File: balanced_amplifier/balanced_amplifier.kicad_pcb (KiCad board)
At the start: 2 copper layers, 100 x 100 mm, 124 parts, among them J1 Molex_SL_01x02_Male, J2 Molex_SL_01x02_Male, J3 Molex_SL_01x03_Male, J4 Molex_SL_01x02_Male, J5 Molex_SL_01x02_Male, J6 Molex_SL_01x02_Male, J7 Molex_SL_01x02_Male, U1 LM4562, U2 LM4562, U3 NE5532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

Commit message: update TODO and date in titleblock
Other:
- board text added: "TODO Update date silk Add license info to silk check pot directions update pot footprints (square pin 1, etc.)"
- board text removed: "TODO Update date silk Add license info to silk Update title block check pot directions update pot footprints (square pin 1, etc.)"
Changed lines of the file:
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@@
   (title_block
     (title "Balanced Amplifier")
-    (date 2019-06-18)
+    (date 2019-06-19)
     (rev 1)
     (company "G. Keeth")
@@
     (arrow2b (pts (xy 65.200001 33.8) (xy 65.786422 34.926504)))
   )
-  (gr_text "TODO\nUpdate date silk\nAdd license info to silk\nUpdate title block\ncheck pot directions\nupdate pot footprints (square pin 1, etc.)" (at 213.2 34.3) (layer Cmts.User)
+  (gr_text "TODO\nUpdate date silk\nAdd license info to silk\ncheck pot directions\nupdate pot footprints (square pin 1, etc.)" (at 213.2 34.3) (layer Cmts.User)
     (effects (font (size 1 1) (thickness 0.15)) (justify left))
   )
@@
   (segment (start 92.66 51.82) (end 93.765 52.925) (width 0.25) (layer F.Cu) (net 37))
   (segment (start 92.66 34.3) (end 92.66 51.82) (width 0.25) (layer F.Cu) (net 37))
-  (segment (start 144.385 48.425) (end 146.05 50.09) (width 0.25) (layer F.Cu) (net 58))
-  (segment (start 146.05 50.965) (end 142.875 54.14) (width 0.25) (layer F.Cu) (net 58))
-  (segment (start 146.05 50.09) (end 146.05 50.965) (width 0.25) (layer F.Cu) (net 58))
-  (segment (start 148.59 48.03) (end 148.985 48.425) (width 0.25) (layer F.Cu) (net 59))
-  (segment (start 147.32 50.09) (end 147.32 54.14) (width 0.25) (layer F.Cu) (net 59))
-  (segment (start 148.985 48.425) (end 147.32 50.09) (width 0.25) (layer F.Cu) (net 59))
-  (segment (start 167.005 50.725) (end 169.305 48.425) (width 0.25) (layer F.Cu) (net 61))
-  (segment (start 167.005 52.87) (end 167.005 50.725) (width 0.25) (layer F.Cu) (net 61))
-  (segment (start 160.96 48.195) (end 160.895 48.26) (width 0.25) (layer F.Cu) (net 60) (status 40000))
-  (segment (start 160.895 48.26) (end 161.76 48.26) (width 0.25) (layer F.Cu) (net 60))
-  (segment (start 162.56 49.06) (end 162.56 53.505) (width 0.25) (layer F.Cu) (net 60))
-  (segment (start 161.76 48.26) (end 162.56 49.06) (width 0.25) (layer F.Cu) (net 60))
   (segment (start 107.735 59.64) (end 107.735 54.675) (width 0.25) (layer F.Cu) (net 38))
   (segment (start 111.125 63.03) (end 107.735 59.64) (width 0.25) (layer F.Cu) (net 38))
@@
   (segment (start 97.79 95.735) (end 97.79 97.32) (width 0.25) (layer F.Cu) (net 57))
   (segment (start 99.38 94.145) (end 97.79 95.735) (width 0.25) (layer F.Cu) (net 57))
+  (segment (start 144.385 48.425) (end 146.05 50.09) (width 0.25) (layer F.Cu) (net 58))
+  (segment (start 146.05 50.965) (end 142.875 54.14) (width 0.25) (layer F.Cu) (net 58))
+  (segment (start 146.05 50.09) (end 146.05 50.965) (width 0.25) (layer F.Cu) (net 58))
   (segment (start 127.16 35.76) (end 127.16 34.3) (width 0.25) (layer F.Cu) (net 58))
   (segment (start 127.7 36.3) (end 127.16 35.76) (width 0.25) (layer F.Cu) (net 58))
@@
   (segment (start 137.7 41.74) (end 144.385 48.425) (width 0.25) (layer F.Cu) (net 58))
   (segment (start 137.7 34.84) (end 137.7 41.74) (width 0.25) (layer F.Cu) (net 58))
+  (segment (start 148.59 48.03) (end 148.985 48.425) (width 0.25) (layer F.Cu) (net 59))
+  (segment (start 147.32 50.09) (end 147.32 54.14) (width 0.25) (layer F.Cu) (net 59))
+  (segment (start 148.985 48.425) (end 147.32 50.09) (width 0.25) (layer F.Cu) (net 59))
   (segment (start 139.7 39.14) (end 148.985 48.425) (width 0.25) (layer F.Cu) (net 59))
   (segment (start 139.7 34.3) (end 139.7 39.14) (width 0.25) (layer F.Cu) (net 59))
@@
   (segment (start 139.7 34.3) (end 139.7 32.7) (width 0.25) (layer F.Cu) (net 59))
   (segment (start 139.7 32.7) (end 138.3 31.3) (width 0.25) (layer F.Cu) (net 59))
+  (segment (start 160.96 48.195) (end 160.895 48.26) (width 0.25) (layer F.Cu) (net 60) (status 40000))
+  (segment (start 160.895 48.26) (end 161.76 48.26) (width 0.25) (layer F.Cu) (net 60))
+  (segment (start 162.56 49.06) (end 162.56 53.505) (width 0.25) (layer F.Cu) (net 60))
+  (segment (start 161.76 48.26) (end 162.56 49.06) (width 0.25) (layer F.Cu) (net 60))
   (segment (start 157.16 44.525) (end 160.895 48.26) (width 0.25) (layer F.Cu) (net 60))
   (segment (start 157.16 34.3) (end 157.16 44.525) (width 0.25) (layer F.Cu) (net 60))
@@
   (segment (start 157.16 34.3) (end 155.2 34.3) (width 0.25) (layer F.Cu) (net 60))
   (segment (start 155.2 34.3) (end 152.2 37.3) (width 0.25) (layer F.Cu) (net 60))
+  (segment (start 167.005 50.725) (end 169.305 48.425) (width 0.25) (layer F.Cu) (net 61))
+  (segment (start 167.005 52.87) (end 167.005 50.725) (width 0.25) (layer F.Cu) (net 61))
   (segment (start 159.7 38.82) (end 169.305 48.425) (width 0.25) (layer F.Cu) (net 61))
   (segment (start 159.7 34.3) (end 159.7 38.82) (width 0.25) (layer F.Cu) (net 61))

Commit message: resize project info silk, update date
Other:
- board text added: "Balanced Amplifier rev1 Preamp 2019 G. Keeth 2019-06-19"
- board text removed: "Balanced Amplifier rev1 Preamp 2019 G. Keeth 2019-06-18"
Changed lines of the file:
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@@
     (effects (font (size 1.3 1.3) (thickness 0.2)))
   )
-  (gr_text "Balanced Amplifier rev1\nPreamp 2019\nG. Keeth 2019-06-18" (at 105.2 45.8) (layer B.SilkS)
-    (effects (font (size 1.5 1.5) (thickness 0.3)) (justify left mirror))
+  (gr_text "Balanced Amplifier rev1\nPreamp 2019\nG. Keeth\n2019-06-19" (at 102.45 43.05) (layer B.SilkS)
+    (effects (font (size 1 1) (thickness 0.15)) (justify left mirror))
   )
   (gr_line (start 176.2 127.8) (end 76.2 127.8) (layer Edge.Cuts) (width 0.15))

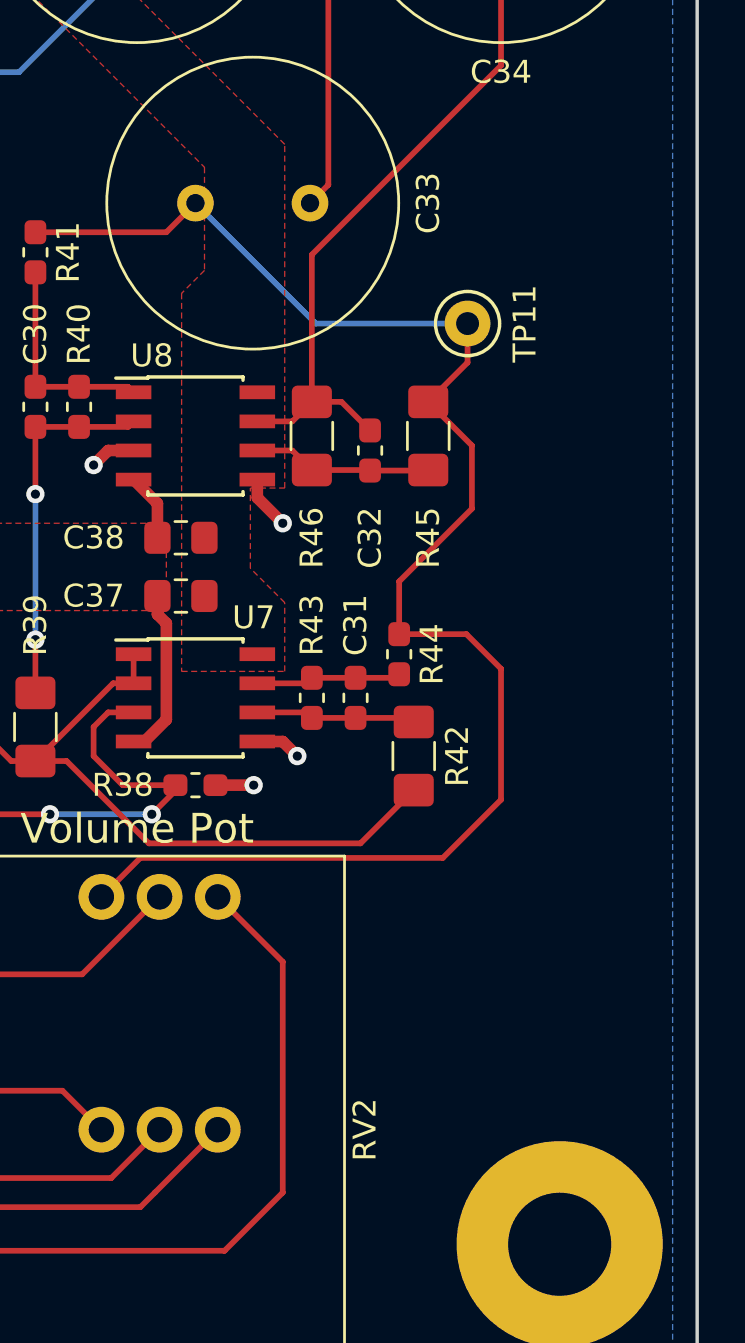
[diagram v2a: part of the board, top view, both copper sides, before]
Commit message: add license info to schematics & layouts, including made with kicad logo, as well as project info to silkscreen
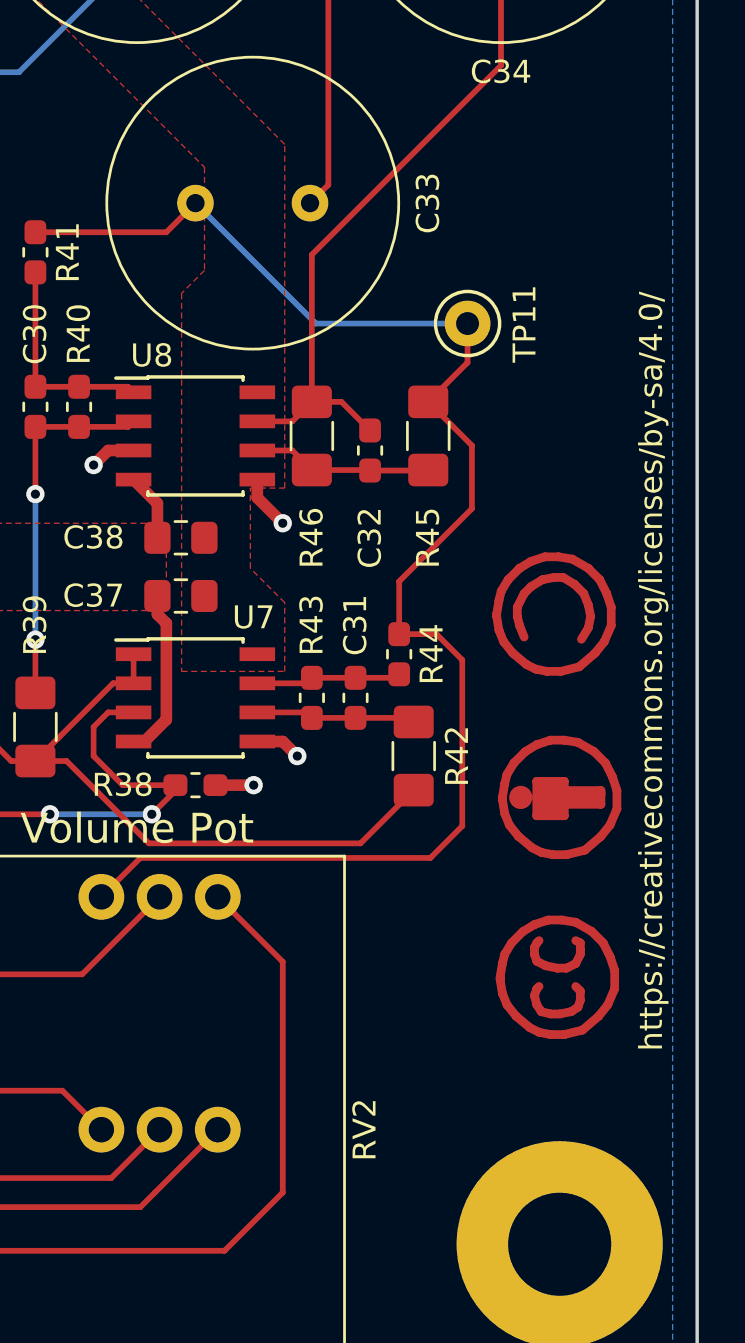
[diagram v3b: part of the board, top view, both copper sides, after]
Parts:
- added REF**: Symbol_CC-ShareAlike_CopperTop_Small, Symbol:Symbol_CC-ShareAlike_CopperTop_Small, F.Cu at (169.9, 94.3)
- added REF**: Symbol_CC-Attribution_CopperTop_Small, Symbol:Symbol_CC-Attribution_CopperTop_Small, F.Cu at (170.2, 102.3)
- added REF**: Symbol_CreativeCommons_CopperTop_Type2_Small, Symbol:Symbol_CreativeCommons_CopperTop_Type2_Small, F.Cu at (170.2, 110.3)
- added REF**: OSHW-Logo2_9.8x8mm_SilkScreen, Symbol:OSHW-Logo2_9.8x8mm_SilkScreen, B.Cu at (162.4, 42.5)
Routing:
- net Net-(C33-Pad2): track 68.5 -> 66.0 mm
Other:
- board text added: "TODO Update date silk check pot directions update pot footprints (square pin 1, etc.)"
- board text added: "https://creativecommons.org/licenses/by-sa/4.0/"
- board text removed: "TODO Update date silk Add license info to silk check pot directions update pot footprints (square pin 1, etc.)"

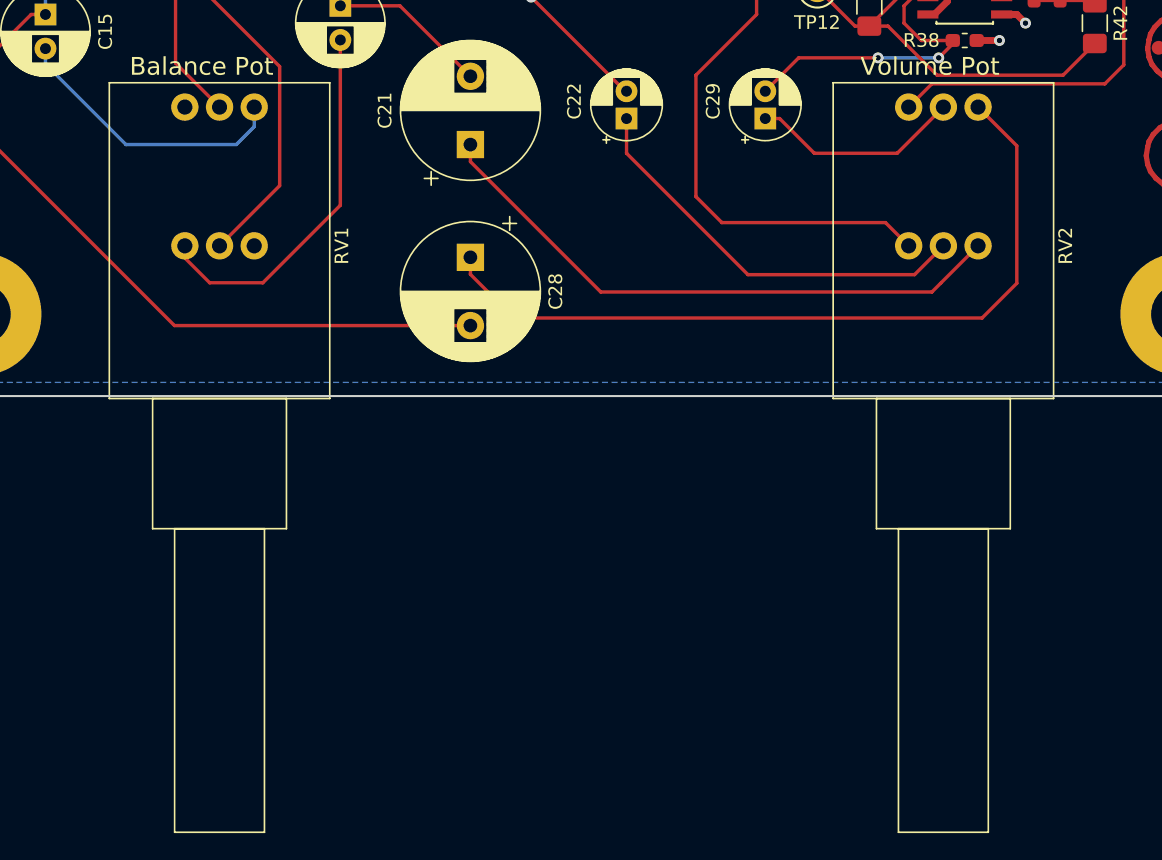
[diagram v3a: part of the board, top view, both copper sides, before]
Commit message: update footprint for volume/balance pots
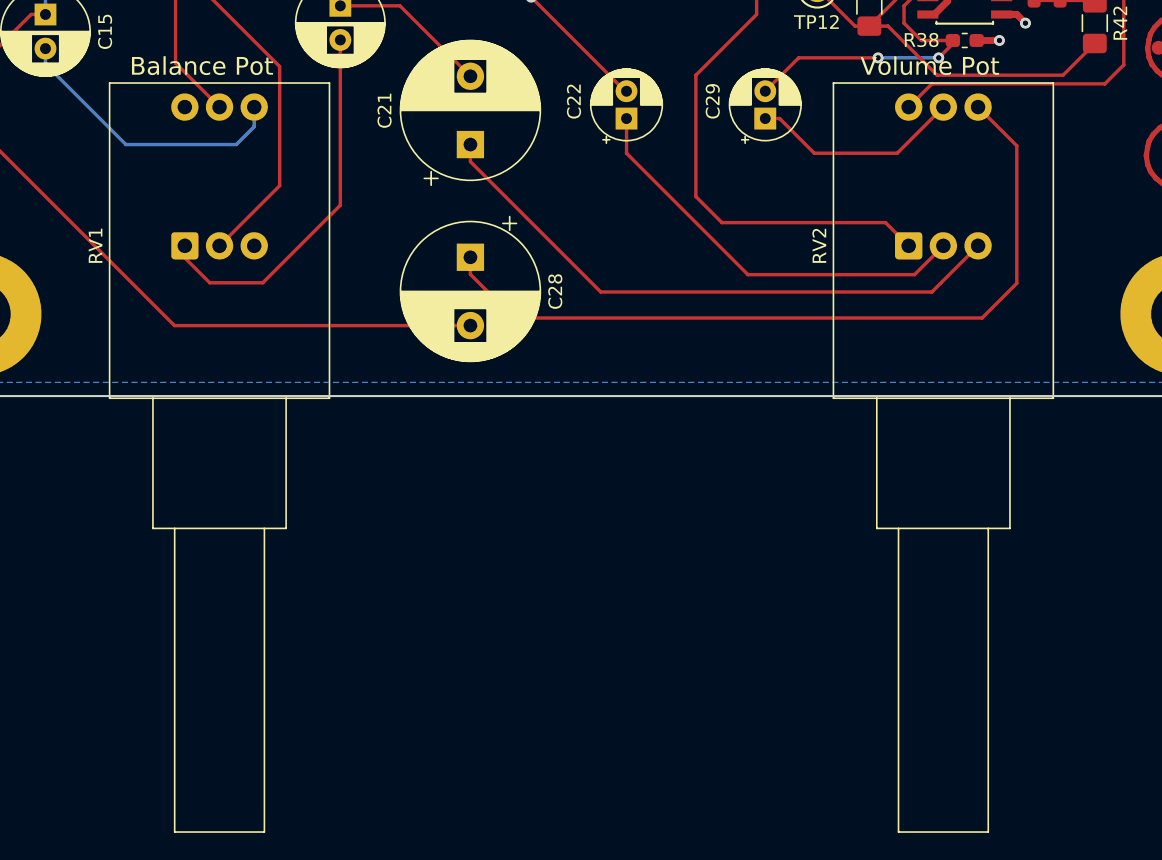
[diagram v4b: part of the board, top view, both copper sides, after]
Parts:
- RV1, RV2: footprint Potentiometer_THT_custom:Potentiometer_Bourns_91_Dual_Horizontal -> Potentiometer_THT_custom:Potentiometer_Bourns_91A2x-x28-xxx_Dual_Horizontal
- turned RV1 to 90 degrees
- turned RV2 to 90 degrees
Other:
- board text added: "TODO Update date silk check pot directions"
- board text removed: "TODO Update date silk check pot directions update pot footprints (square pin 1, etc.)"
